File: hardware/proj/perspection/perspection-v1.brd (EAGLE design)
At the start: 90 x 70 mm, 233 parts, among them J1 MICRO-USB-10118192-0001LF, J2 1X6-PTSA_1.5/6-3.5-Z, J3 1X2-PTSA_1.5/2-3.5-Z, J4 1X2-JST-PH-SMD, J5 1X2-0428202213, J6 JTAG-ARM_TC-10, J7 JTAG-ARM_TC-10, J8 1X3-0.1IN_THRUHOLE, Q1 NMOS-CSD18533Q5A, Q10 NMOS-CSD18533Q5A, Q11 IRFML8244TRPBF, Q2 NMOS-CSD18533Q5A, Q3 NMOS-CSD18533Q5A, Q4 NMOS-CSD18533Q5A, Q5 NMOS-CSD18533Q5A, Q6 NMOS-CSD18533Q5A, Q7 NMOS-CSD18533Q5A, Q8 BSS138L, Q9 BSS138L, U1 ATUM, U10 DRV8301DCAR, U11 OPA2374AIDCNR, U12 OPA170AIDBVR, U13 BNO055, U2 FT232RQ, U3 TPS79933DDCR, U4 MCP73831T-2ACI/OT, U5 TMS320F28069MPZT, U6 DRV8801PWPR, U7 DRV8801PWPR, U8 DRV8801PWPR, U9 DRV8801PWPR, Y1 32.768kHz

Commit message: TAKE THIS SHIT JASON
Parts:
- S1: value TACTILE-SWITCH-SMD -> TACTILE-SWITCH-EVQP2; device perspection:TACTILE-SWITCH-SMD -> perspection:EVQP2
- moved Q7 198.4 mm to (-154.0, 73.0)
- moved R72 168.1 mm to (53.0, 21.0)
- moved L4 166.5 mm to (13.0, -41.5), turned to 180 degrees
- moved C49 165.9 mm to (65.6, 36.9), turned to 90 degrees
- moved R70 159.0 mm to (50.0, 20.0)
- moved U12 157.2 mm to (-169.0, 63.0)
- moved C46 157.1 mm to (64.2, 37.3), turned to 90 degrees
- moved R44 156.5 mm to (15.0, -35.5)
- moved R68 153.3 mm to (50.0, 18.0)
- moved R43 152.6 mm to (15.0, -33.5)
- moved C35 150.4 mm to (67.3, 13.0), turned to 90 degrees
- moved R78 149.3 mm to (-1.00, -49.0), turned to 90 degrees
- moved C44 148.0 mm to (54.4, 24.6), turned to 180 degrees
- moved C65 145.4 mm to (66.0, 10.5)
- moved C62 145.2 mm to (68.0, -4.00)
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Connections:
- net N$16 renamed SENSE1
- net N$17 renamed _VPROPI1
- net N$21 renamed SENSE2
- net N$25 renamed SENSE3
- net N$26 renamed _VPROPI2
- net N$27 renamed _VPROPI3
- net N$31 renamed AUX_SENSE
- net N$32 renamed _AUX_VPROPI
- net N$64 renamed M1+
- net N$65 renamed M1-
- net N$66 renamed M2+
- net N$67 renamed M2-
- net N$68 renamed M3+
- net N$69 renamed M3-
- net N$70 renamed M_AUX+
- net N$71 renamed M_AUX-
- net !PICCOLO_RESET: now also S1.2; no longer S1.3
- net GND: now also S1.3; no longer S1.2
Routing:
- net N$51: track 0.00 -> 11.7 mm
- net N$58: track 0.00 -> 11.3 mm
- net GND: track 9.96 -> 20.0 mm, vias 90 -> 91
- net C_ISENSE_P: track 0.00 -> 6.84 mm, vias 0 -> 2
- net C_ISENSE_N: track 0.00 -> 6.84 mm, vias 0 -> 2
- net +3V3: track 13.8 -> 18.4 mm, vias 16 -> 17
- net __IB_FB: track 0.00 -> 2.50 mm
- net N$24: track 0.00 -> 2.43 mm
- net N$20: track 0.00 -> 2.43 mm
- net N$30: track 0.00 -> 2.41 mm
- net N$15: track 0.00 -> 2.41 mm
- net _DRV_SDO: track 0.00 -> 2.29 mm
- net __IA_FB: track 0.00 -> 2.06 mm
- net _VB_FB: track 0.00 -> 2.06 mm
- net _DRV_SDI: track 0.00 -> 2.06 mm
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- added copper zone on layer 1, net AUX_SENSE
- added copper zone on layer 1, net SENSE1
- added copper zone on layer 1, net SENSE2
- added copper zone on layer 1, net SENSE3

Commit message: holy fucking shit 81 airwires to go
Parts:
- added J9: 1X2-PTSA_1.5/2-3.5-Z, perspection:3.5MM_PTSA_1.5/2-3.5-Z
- moved R16 210.8 mm to (66.9, 10.5), flipped to the bottom, turned to 270 degrees
- moved C19 210.0 mm to (66.6, 7.10), flipped to the bottom
- moved U12 208.9 mm to (38.7, 40.7)
- moved R80 205.7 mm to (36.2, 43.1)
- moved C17 205.2 mm to (64.0, 1.80), flipped to the bottom
- moved Q8 205.2 mm to (29.6, 41.4), turned to 90 degrees
- moved C83 205.0 mm to (64.4, 6.10), turned to 270 degrees
- moved U8 203.8 mm to (63.3, 6.20), flipped to the bottom
- moved C18 202.8 mm to (62.8, 1.00), flipped to the bottom
- moved C93 201.8 mm to (36.6, 41.5), turned to 270 degrees
- moved R14 200.2 mm to (61.5, 1.50), flipped to the bottom
- moved R17 199.0 mm to (61.5, 10.8), flipped to the bottom, turned to 180 degrees
- moved C22 198.7 mm to (60.7, 1.50), flipped to the bottom
- moved R79 195.5 mm to (31.8, 45.1), turned to 90 degrees
- moved R81 195.2 mm to (33.2, 45.1), turned to 270 degrees
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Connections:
- net N$6 renamed D_P
- net N$7 renamed D_N
- new net N$16: C69.1, U5.81
- new net N$17: C68.1, U5.63
- new net N$21: C66.1, U5.14
- new net N$6: C71.1, U5.3
- new net N$7: C70.1, U5.91
- net +12V: now also J9.1
- net +12V_GND: now also J9.2
- net N$58: no longer C66.1, C68.1, C69.1, C70.1, C71.1, U5.14, U5.3, U5.63, U5.81, U5.91
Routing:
- net +12V: track 22.0 -> 100.5 mm, vias 92 -> 96
- net !ATUM_RESET: track 0.00 -> 63.5 mm, vias 0 -> 3
- net N$93: track 0.00 -> 36.2 mm, vias 0 -> 2
- net N$95: track 0.00 -> 36.0 mm, vias 0 -> 2
- net VBAT: track 0.00 -> 35.8 mm
- net !DTR_FTDI: track 0.00 -> 34.1 mm, vias 0 -> 1
- net N$94: track 0.00 -> 29.1 mm, vias 0 -> 2
- net !PICCOLO_RESET: track 0.00 -> 27.4 mm, vias 0 -> 2
- net BOOTLOADER_CTRL: track 0.00 -> 27.3 mm, vias 0 -> 1
- net N$91: track 0.00 -> 24.0 mm
- net M_AUX+: track 0.00 -> 23.3 mm
- net !RTS_FTDI: track 0.00 -> 22.8 mm, vias 0 -> 1
- net N$92: track 0.00 -> 22.8 mm, vias 0 -> 2
- net +3V3: track 18.4 -> 40.3 mm, vias 17 -> 46
- net BOOTLOADER_RX: track 0.00 -> 20.8 mm
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- added copper zone on layer 1, net M_AUX+
- added copper zone on layer 1, net M_AUX-
- added copper zone on layer 1, net N$51
- added copper zone on layer 1, net N$59
- added copper zone on layer 1, net N$60
- added copper zone on layer 16, net SENSE1
- added copper zone on layer 16, net SENSE2
- added copper zone on layer 16, net SENSE3
- removed copper zone on layer 1, net SENSE1
- removed copper zone on layer 1, net SENSE2
- removed copper zone on layer 1, net SENSE3
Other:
- outline, holes or cut-outs redrawn

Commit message: small change. holy fucking shit so tight
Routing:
- net !ATUM_RESET: track 63.5 -> 59.9 mm
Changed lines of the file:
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@@
 <wire x1="4" y1="29" x2="4" y2="31.3" width="0.127" layer="1"/>
 <via x="4" y="31.3" extent="1-16" drill="0.2"/>
-<wire x1="4" y1="31.3" x2="4" y2="45.3" width="0.127" layer="16"/>
-<wire x1="4" y1="45.3" x2="6.2" y2="47.5" width="0.127" layer="16"/>
-<wire x1="6.2" y1="47.5" x2="12.4" y2="47.5" width="0.127" layer="16"/>
 <wire x1="12.4" y1="47.5" x2="15.9" y2="51" width="0.127" layer="16"/>
 <via x="15.9" y="51" extent="1-16" drill="0.2"/>
@@
 <wire x1="15.4" y1="51.5" x2="13" y2="51.5" width="0.127" layer="1"/>
 <wire x1="13" y1="51.5" x2="12.2" y2="52.3" width="0.127" layer="1"/>
+<wire x1="4" y1="31.3" x2="4" y2="32" width="0.127" layer="16"/>
+<wire x1="4" y1="32" x2="12.4" y2="40.4" width="0.127" layer="16"/>
+<wire x1="12.4" y1="40.4" x2="12.4" y2="47.5" width="0.127" layer="16"/>
 </signal>
 <signal name="BOOTLOADER_CTRL">

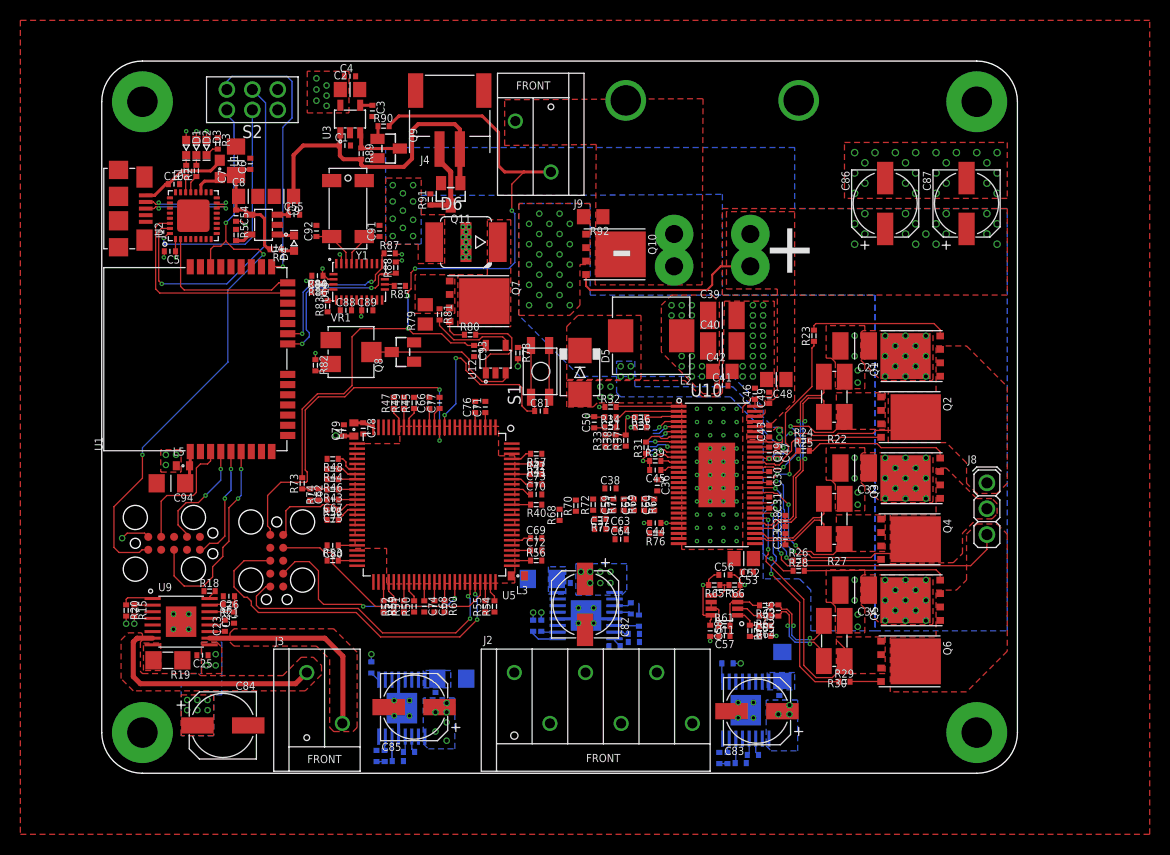
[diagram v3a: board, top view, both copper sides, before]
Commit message: 26 airwires!
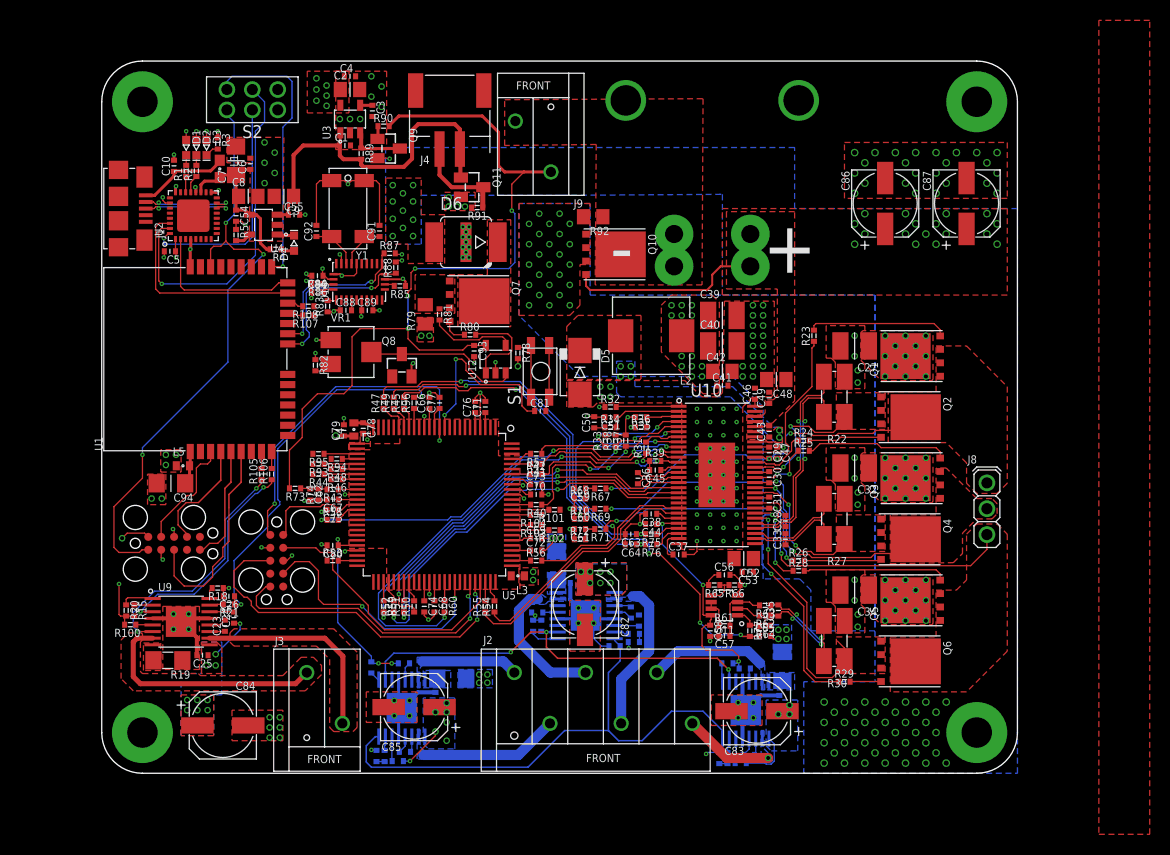
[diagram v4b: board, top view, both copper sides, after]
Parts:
- added R100, R97, R98, R99: 10k, perspection:R0402
- added R101, R102, R103, R104, R105, R106, R107, R108, R93, R94, R95, R96: 0, perspection:R0402
- moved C37 8.10 mm to (56.7, 21.5)
- moved C60 7.31 mm to (47.0, 26.0), turned to 180 degrees
- moved C61 5.82 mm to (47.0, 24.0), turned to 180 degrees
- moved R75 5.22 mm to (54.0, 23.5)
- moved C38 4.72 mm to (54.0, 25.5), turned to 180 degrees
- moved R91 4.67 mm to (36.9, 55.6), turned to 180 degrees
- moved R67 4.59 mm to (49.0, 28.0), turned to 180 degrees
- moved C59 3.67 mm to (47.0, 28.0), turned to 180 degrees
- moved R72 3.64 mm to (47.0, 23.0), turned to 0 degrees
- moved R68 2.56 mm to (47.0, 27.0), turned to 0 degrees
- moved R71 2.42 mm to (49.0, 24.0), turned to 180 degrees
- moved R69 2.33 mm to (49.0, 26.0), turned to 180 degrees
- moved Q11 2.21 mm to (36.4, 57.6), turned to 270 degrees
- moved C36 2.02 mm to (52.7, 29.0)
- moved R12 1.91 mm to (44.7, 20.4), turned to 270 degrees
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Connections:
- net N$16 renamed VDD4
- net N$17 renamed VDD3
- net N$21 renamed VDD1
- net N$58 renamed VDD2
- net N$6 renamed VDD6
- net N$7 renamed VDD5
- removed net ATUM_B3: U1.9
- removed net ATUM_B4: U1.8
- new net ATUM_ENCODER_A: R107.1
- new net ATUM_ENCODER_B: R108.1
- new net N$25: R93.1, U5.30
- new net N$26: R94.1, U5.29
- new net N$27: R95.1, U5.28
- new net N$31: R96.1, U5.17
- new net N$32: R102.2, U5.83
- new net N$43: R103.2, U5.84
- new net N$44: R104.2, U5.86
- new net N$46: R101.2, U5.87
- new net N$47: R105.2, U1.8
- new net N$48: R106.2, U1.9
- net !AUX_SLEEP: now also R100.1
- net !SLEEP1: now also R99.1
- net !SLEEP2: now also R97.1
- net !SLEEP3: now also R98.1
- net +3V3: now also R100.2, R97.2, R98.2, R99.2
- net ATUM_C0: now also R108.2
- net ATUM_C1: now also R107.2
- net AUX_ENABLE: now also R101.1, R105.1
- net AUX_PHASE: now also R106.1
- net AUX_VPROPI: now also R96.2
- net ENABLE1: now also R104.1
- net ENABLE2: now also R103.1
- net ENABLE3: now also R102.1
- net VPROPI1: now also R95.2
- net VPROPI2: now also R94.2
- net VPROPI3: now also R93.2
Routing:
- net GND: track 28.2 -> 139.5 mm, vias 93 -> 173
- net MODE2: track 0.95 -> 52.8 mm
- net IC_FB: track 0.97 -> 52.9 mm, vias 0 -> 4
- net DC_CAL: track 1.80 -> 45.9 mm, vias 0 -> 4
- net MODE1: track 1.63 -> 41.9 mm, vias 0 -> 3
- net EN_GATE: track 0.00 -> 38.1 mm, vias 0 -> 2
- net PWM_BH: track 0.00 -> 37.5 mm, vias 0 -> 2
- net IA_FB: track 0.00 -> 37.1 mm, vias 0 -> 2
- net PWM_AH: track 0.00 -> 37.0 mm, vias 0 -> 2
- net +3V3: track 40.3 -> 76.6 mm, vias 46 -> 48
- net DRV_SDO: track 3.04 -> 39.3 mm, vias 1 -> 4
- net PWM_AL: track 0.00 -> 36.1 mm, vias 0 -> 2
- net AUX_VPROPI: track 0.80 -> 36.8 mm, vias 0 -> 2
- net VB_FB: track 0.00 -> 29.3 mm, vias 0 -> 2
- net !DRV_CS: track 3.05 -> 29.2 mm, vias 1 -> 2
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- added copper zone on layer 15, net +12V
- added copper zone on layer 16, net M1+
- added copper zone on layer 16, net M1-
- added copper zone on layer 16, net M2+
- added copper zone on layer 16, net M2-
- added copper zone on layer 16, net M3+
- added copper zone on layer 16, net M3-

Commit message: no airwires! for now...
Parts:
- moved Q8 1.56 mm to (30.6, 41.2), turned to 90 degrees
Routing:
- net VPROPI3: track 0.80 -> 69.7 mm, vias 0 -> 1
- net VPROPI2: track 0.80 -> 54.3 mm, vias 0 -> 3
- net AUX_ENABLE: track 24.0 -> 77.0 mm, vias 2 -> 4
- net IB_FB: track 3.20 -> 54.1 mm, vias 1 -> 2
- net PWM_BL: track 0.00 -> 47.6 mm, vias 0 -> 2
- net VC_FB: track 1.90 -> 47.8 mm, vias 0 -> 4
- net VA_FB: track 1.90 -> 45.8 mm, vias 0 -> 2
- net VPROPI1: track 0.80 -> 35.8 mm, vias 0 -> 3
- net ENABLE3: track 0.00 -> 29.7 mm, vias 0 -> 3
- net ENABLE2: track 0.00 -> 23.4 mm, vias 0 -> 3
- net ENABLE1: track 0.00 -> 23.4 mm, vias 0 -> 1
- net +12V: track 116.4 -> 120.0 mm, vias 142 -> 146
- net GND: track 139.5 -> 142.8 mm, vias 173 -> 174
- net N$95: track 34.1 -> 32.1 mm
- net N$91: track 27.1 -> 28.6 mm

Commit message: JASON TAKE THE WHEEL
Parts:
- added C95: 4.7uF, perspection:C0603
- added J10: 1X5, perspection:1X5_0.1IN_THRUHOLE
- added R109, R111, R113: 23.2k, perspection:R0402
- added R110, R112, R114: 45.2k, perspection:R0402
- added R115, R116, R117, R118: 0, perspection:R0402
- added R119, R120, R121, R122: (no value), perspection:R0402
- added U14: TPS81256, perspection:TI-SIP-9
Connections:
- net N$91 renamed PICCOLO_TMS
- net N$92 renamed PICCOLO_TCK
- net N$93 renamed PICCOLO_TDI
- net N$95 renamed !PICCOLO_TRST
- removed net ATUM_C2: U1.19
- removed net ATUM_ENCODER_A: R107.1
- removed net ATUM_ENCODER_B: R108.1
- removed net N$94: J7.6, U5.70
- new net !SPI_CS: R117.2, U1.19
- new net ENC_PWR: C95.1, J10.2, U14.A3, U14.B3, U14.C3
- new net EQEP1A: R107.1, R111.1, R112.2, U5.6
- new net EQEP1B: R108.1, R109.1, R110.2, U5.7
- new net EQEP1I: R113.1, R114.2, U5.2
- new net GPIO_34: R121.1, R122.2, U5.68
- new net N$16: J10.3, R111.2
- new net N$17: J10.4, R113.2
- new net N$6: J10.1, R109.2
- new net PICCOLO_TDO: J7.6, R119.1, R120.2, U5.70
- new net _!SPI_CS: R117.1, U5.89
- new net _SPI_MISO: R116.1, U5.75
- new net _SPI_MOSI: R115.1, U5.69
- new net _SPI_SCK: R118.1, U5.85
- net +3V3: now also R119.2, R121.2, U14.B2, U14.C1, U14.C2
- net GND: now also C95.2, J10.5, R110.1, R112.1, R114.1, R120.1, R122.1, U14.A1, U14.A2, U14.B1
- net SPI_MISO: now also R116.2
- net SPI_MOSI: now also R115.2
- net SPI_SCK: now also R118.2
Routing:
- net N$16: track 0.00 -> 54.0 mm, vias 0 -> 3
- net N$6: track 0.00 -> 49.2 mm, vias 0 -> 5
- net _!SPI_CS: track 0.00 -> 35.7 mm, vias 0 -> 2
- net PICCOLO_TDO: track 0.00 -> 34.7 mm, vias 0 -> 3
- net EQEP1I: track 0.00 -> 32.6 mm, vias 0 -> 2
- net N$94: track 29.1 -> 0.00 mm, vias 2 -> 0
- net EQEP1B: track 0.00 -> 24.5 mm, vias 0 -> 3
- net EQEP1A: track 0.00 -> 23.8 mm, vias 0 -> 3
- net ENC_PWR: track 0.00 -> 14.2 mm
- net GND: track 142.8 -> 152.5 mm, vias 174 -> 178
- net N$17: track 0.00 -> 7.69 mm, vias 0 -> 2
- net +3V3: track 76.6 -> 82.2 mm, vias 48 -> 50
- net PICCOLO_TDI: track 36.2 -> 30.9 mm, vias 2 -> 4
- net M_AUX-: track 20.4 -> 16.5 mm
- net ATUM_TDO: track 11.6 -> 14.8 mm, vias 0 -> 2
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- added copper zone on layer 1, net ENC_PWR

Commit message: blarg
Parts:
- added C96: 0.1uF, perspection:C0402
- added R123: 0, perspection:R0402
- moved R18 2.20 mm to (9.20, 18.1), turned to 0 degrees
- moved S2 1.36 mm to (15.9, 67.0)
- moved C10 1.00 mm to (6.10, 59.6)
- moved C5 0.10 mm to (6.70, 51.4)
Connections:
- removed net ATUM_ADC3: U1.25
- new net N$7: C96.1, R123.1, U1.25
- net AUX_VPROPI: now also R123.2
- net GND: now also C96.2
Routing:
- net N$51: track 19.4 -> 90.1 mm
- net AUX_VPROPI: track 36.8 -> 80.8 mm, vias 2 -> 4
- net _SPI_SCK: track 0.00 -> 34.6 mm, vias 0 -> 4
- net _SPI_MISO: track 0.00 -> 33.1 mm, vias 0 -> 4
- net _SPI_MOSI: track 0.00 -> 29.3 mm, vias 0 -> 4
- net ENABLE2: track 23.8 -> 29.0 mm
- net !ATUM_RESET: track 59.9 -> 64.9 mm
- net N$7: track 0.00 -> 4.87 mm
- net IB_FB: track 53.9 -> 57.7 mm
- net ENABLE1: track 23.2 -> 26.9 mm
- net !PICCOLO_TRST: track 32.0 -> 33.9 mm
- net !RTS_FTDI: track 22.8 -> 24.1 mm
- net GND: track 152.5 -> 153.7 mm, vias 178 -> 180
- net !DTR_FTDI: track 34.1 -> 35.1 mm
- net BOOTLOADER_CTRL: track 27.3 -> 28.2 mm
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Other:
- board text added: "PWR"
- board text added: "RX"
- board text added: "TX"
